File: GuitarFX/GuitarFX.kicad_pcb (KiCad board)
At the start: 4 copper layers, 149 parts, among them IC401 PCM3060PWR, J202 Screw_Terminal_01x02, J301 USB_C_Receptacle_USB2.0, J302 Conn_ARM_SWD_TagConnect_TC2030, J303 Screw_Terminal_01x06, J401 Screw_Terminal_01x04, SW301 SW_SPDT, U201 NCP718xSN500, U202 NCP1117-3.3_SOT223, U301 USBLC6-2SC6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

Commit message: Finished rough layout for MCU
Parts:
- C302: footprint Capacitor_SMD:C_0603_1608Metric -> Capacitor_SMD:C_0402_1005Metric
- moved U301 147.8 mm to (211.2, 48.5), turned to 180 degrees
- moved J301 129.8 mm to (219.2, 48.2), turned to 90 degrees
- moved C319 128.8 mm to (194.8, 53.0), turned to 135 degrees
- moved C318 123.9 mm to (200.2, 69.5), turned to -135 degrees
- moved R311 123.3 mm to (199.0, 57.2), turned to 45 degrees
- moved R310 122.2 mm to (200.2, 58.5), turned to 45 degrees
- moved R309 121.3 mm to (201.5, 59.8), turned to 45 degrees
- moved R304 120.2 mm to (212.9, 45.5), turned to 90 degrees
- moved C317 120.0 mm to (205.5, 55.2), turned to 135 degrees
- moved D302 118.0 mm to (182.4, 53.7), turned to 135 degrees
- moved R305 117.8 mm to (185.2, 50.7), turned to 135 degrees
- moved R 117.6 mm to (183.9, 52.0), turned to 135 degrees
- moved C306 116.6 mm to (202.0, 67.3), turned to -135 degrees
- moved R303 115.2 mm to (212.9, 51.5), turned to -90 degrees
- moved R307 114.6 mm to (180.7, 55.2), turned to 135 degrees
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- renumbered R306 to R

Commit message: Changed to mono input, and finished rough Analog Frontend layout
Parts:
- removed C411, C417, C425, C435: 1n, Capacitor_SMD:C_0603_1608Metric
- removed C412, C413, C426, C427: 100n, Capacitor_SMD:C_0402_1005Metric
- removed C414: 10n, Capacitor_SMD:C_0402_1005Metric
- removed C415, C434: 4.7u, Capacitor_SMD:C_0603_1608Metric
- removed C416, C418, C436: 150p, Capacitor_SMD:C_0603_1608Metric
- removed D402, D404: SMAJ15A, Diode_SMD:D_SMA
- removed R: 33R, Resistor_SMD:R_0603_1608Metric
- removed R411: 1k, Resistor_SMD:R_0402_1005Metric
- removed R412, R430: 8.2k, Resistor_SMD:R_0402_1005Metric
- removed R413, R431: 27k, Resistor_SMD:R_0402_1005Metric
- removed R414, R432: 15k, Resistor_SMD:R_0402_1005Metric
- removed R415, R433: 100R, Resistor_SMD:R_0402_1005Metric
- removed R416: 1M, Resistor_SMD:R_0402_1005Metric
- removed R434: 10k, Resistor_SMD:R_0402_1005Metric
- removed U404, U405, U408, U409: TLV9161IDBVR, TLV9161IDBVR:SOT95P280X145-5N
- added J402: Screw_Terminal_01x02, TerminalBlock_Phoenix:TerminalBlock_Phoenix_MPT-0,5-2-2.54_1x02_P2.54mm_Horizontal, F.Cu at (168.0, 105.4)
- added R306: 33R, Resistor_SMD:R_0603_1608Metric, F.Cu at (184.0, 52.0)
- C401, C419: footprint Capacitor_SMD:C_0603_1608Metric -> Capacitor_SMD:C_0402_1005Metric
- J401: value Screw_Terminal_01x04 -> Screw_Terminal_01x02; footprint TerminalBlock_Phoenix:TerminalBlock_Phoenix_MPT-0,5-4-2.54_1x04_P2.54mm_Horizontal -> TerminalBlock_Phoenix:TerminalBlock_Phoenix_MPT-0,5-2-2.54_1x02_P2.54mm_Horizontal
- R405, R406, R407, R421, R422, R423: footprint Resistor_SMD:R_0402_1005Metric -> Resistor_SMD:R_0603_1608Metric
- R410: value 1M -> 100k
- R417, R418: value 4.7k -> 10k
- moved C408 126.3 mm to (208.2, 110.9)
- moved C409 119.4 mm to (201.5, 111.7), turned to -90 degrees
- moved U402 116.9 mm to (204.8, 108.2)
- moved C401 112.2 mm to (192.2, 108.2), turned to -90 degrees
- moved C407 111.2 mm to (193.2, 105.7)
- moved C410 110.7 mm to (194.5, 107.9)
- moved R404 110.5 mm to (208.2, 108.2), turned to 180 degrees
- moved R409 109.8 mm to (208.2, 109.4), turned to 180 degrees
- moved U403 109.8 mm to (198.2, 108.2)
- moved R402 108.7 mm to (203.5, 111.0), turned to 180 degrees
- moved D401 108.6 mm to (211.8, 108.2), turned to -90 degrees
- moved J401 107.6 mm to (217.8, 108.3), turned to 90 degrees
- moved R405 103.6 mm to (201.5, 108.5), turned to -90 degrees
- moved R406 101.5 mm to (199.0, 110.9), turned to 180 degrees
- moved C430 100.8 mm to (192.7, 98.5), turned to 180 degrees
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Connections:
- net /Codec/AUDIO_VOUTL renamed /Codec/AUDIO_VOUT
- net /Codec/CODEC_VOUTL renamed /Codec/CODEC_VOUT
- net /Codec/IN_AA_BUFF_IN_L renamed /Codec/IN_AA_BUFF_IN
- net /Codec/IN_AA_BUFF_OUT_L renamed /Codec/IN_AA_BUFF_OUT
- net /Codec/IN_BUF_IN_L renamed /Codec/IN_BUF_IN
- net /Codec/IN_BUF_OUT_L renamed /Codec/IN_BUF_OUT
- net /Codec/IN_RF_L renamed /Codec/IN_RF
- net /Codec/OUT_AA_BUFF_IN_L renamed /Codec/OUT_AA_BUFF_IN
- net /Codec/OUT_AA_BUFF_OUT_L renamed /Codec/OUT_AA_BUFF_OUT
- net Net-(U406--) renamed /Codec/OUT_BUF_OUT
- C407 pad 1: /Codec/CODEC_VINL -> /Codec/CODEC_VIN
- D401 pad 1: /Codec/AUDIO_VINL -> /Codec/AUDIO_VIN
- IC401 pad 18: /Codec/CODEC_VOUTR -> Net-(IC401-VOUTR+)
- IC401 pad 25: /Codec/CODEC_VINL -> /Codec/CODEC_VIN
- IC401 pad 26: /Codec/CODEC_VINR -> /Codec/CODEC_VIN
- J401 pad 2: /Codec/AUDIO_VINR -> /Codec/AUDIO_VIN
- R404 pad 1: /Codec/AUDIO_VINL -> /Codec/AUDIO_VIN
- R410 pad 1: /Codec/IN_BUF_IN_R -> Net-(IC401-VOUTR+)
- R410 pad 2: VCOM -> GND

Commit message: Finished rough layout
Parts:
- removed D301: SMAJ15A, Diode_SMD:D_SMA
- C409: footprint Capacitor_SMD:C_0603_1608Metric -> Capacitor_SMD:C_0402_1005Metric
- R201: footprint Resistor_SMD:R_0603_1608Metric -> Resistor_SMD:R_0805_2012Metric
- moved FB302 83.4 mm to (164.2, 75.7), turned to 180 degrees
- moved C313 82.9 mm to (163.8, 69.9)
- moved C311 76.5 mm to (165.2, 77.7), turned to -90 degrees
- moved R401 76.5 mm to (152.0, 123.9), turned to 90 degrees
- moved U401 76.2 mm to (154.5, 122.8), turned to -90 degrees
- moved C312 76.1 mm to (163.2, 77.7), turned to -90 degrees
- moved R403 71.8 mm to (152.0, 121.7), turned to 90 degrees
- moved C405 69.3 mm to (154.5, 119.4)
- moved R421 68.1 mm to (136.0, 130.9), turned to -90 degrees
- moved C419 67.9 mm to (126.8, 130.7), turned to -90 degrees
- moved R422 67.6 mm to (133.5, 133.4), turned to 180 degrees
- moved C424 64.6 mm to (129.0, 130.4)
- moved C422 64.2 mm to (127.8, 128.2)
- moved R423 64.1 mm to (129.8, 132.9), turned to 90 degrees
- moved R410 62.6 mm to (140.8, 120.9), turned to 180 degrees
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
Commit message: Added mounting holes
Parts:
- added H101: MountingHole_Pad, MountingHole:MountingHole_3.2mm_M3_Pad, F.Cu at (115.0, 63.5)
- added H102: MountingHole_Pad, MountingHole:MountingHole_3.2mm_M3_Pad, F.Cu at (175.0, 63.5)
- added H103: MountingHole_Pad, MountingHole:MountingHole_3.2mm_M3_Pad, F.Cu at (175.0, 138.5)
- added H104: MountingHole_Pad, MountingHole:MountingHole_3.2mm_M3_Pad, F.Cu at (115.0, 138.5)
- moved C311 1.39 mm to (165.2, 79.0)
- moved C312 1.39 mm to (163.2, 79.0)
- moved C313 1.39 mm to (163.8, 71.3)
- moved FB302 1.39 mm to (164.2, 77.0)
- moved FL301 1.39 mm to (159.9, 73.9)
- moved J301 1.39 mm to (173.0, 73.5)
- moved R303 1.39 mm to (166.7, 76.8)
- moved R304 1.39 mm to (166.7, 70.8)
- moved U301 1.39 mm to (164.9, 73.8)
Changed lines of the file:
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@@
     )
   )
+  (footprint "MountingHole:MountingHole_3.2mm_M3_Pad" (layer "F.Cu")
+    (at 175 63.5)
+    (descr "Mounting Hole 3.2mm, M3")
+    (tags "mounting hole 3.2mm m3")
+    (property "Sheetfile" "GuitarFX.kicad_sch")
+    (property "Sheetname" "")
+    (property "ki_description" "Mounting Hole with connection")
+    (property "ki_keywords" "mounting hole")
+    (attr exclude_from_pos_files)
+    (fp_text reference "H102" (at 0 -4.2) (layer "F.SilkS") hide
+        (effects (font (size 1 1) (thickness 0.15)))
+    )
+    (fp_text value "MountingHole_Pad" (at 0 4.2) (layer "F.Fab")
+        (effects (font (size 1 1) (thickness 0.15)))
+    )
+    (fp_text user "${REFERENCE}" (at 0 0) (layer "F.Fab")
+        (effects (font (size 1 1) (thickness 0.15)))
+    )
+    (fp_circle (center 0 0) (end 3.2 0)
+      (stroke (width 0.15) (type solid)) (fill none) (layer "Cmts.User"))
+    (fp_circle (center 0 0) (end 3.45 0)
+      (stroke (width 0.05) (type solid)) (fill none) (layer "F.CrtYd"))
+    (pad "1" thru_hole circle (at 0 0) (size 6.4 6.4) (drill 3.2) (layers "*.Cu" "*.Mask")
+      (net 2 "GND") (pinfunction "1") (pintype "input"))
+  )
   (footprint "Resistor_SMD:R_0402_1005Metric" (layer "F.Cu")
     (at 164.04 131.365 180)
@@
     )
   )
+  (footprint "MountingHole:MountingHole_3.2mm_M3_Pad" (layer "F.Cu")
+    (at 175 138.5)
+    (descr "Mounting Hole 3.2mm, M3")
+    (tags "mounting hole 3.2mm m3")
+    (property "Sheetfile" "GuitarFX.kicad_sch")
+    (property "Sheetname" "")
+    (property "ki_description" "Mounting Hole with connection")
+    (property "ki_keywords" "mounting hole")
+    (attr exclude_from_pos_files)
+    (fp_text reference "H103" (at 0 -4.2) (layer "F.SilkS") hide
+        (effects (font (size 1 1) (thickness 0.15)))
+    )
+    (fp_text value "MountingHole_Pad" (at 0 4.2) (layer "F.Fab")
+        (effects (font (size 1 1) (thickness 0.15)))
+    )
+    (fp_text user "${REFERENCE}" (at 0 0) (layer "F.Fab")
+        (effects (font (size 1 1) (thickness 0.15)))
+    )
+    (fp_circle (center 0 0) (end 3.2 0)
+      (stroke (width 0.15) (type solid)) (fill none) (layer "Cmts.User"))
+    (fp_circle (center 0 0) (end 3.45 0)
+      (stroke (width 0.05) (type solid)) (fill none) (layer "F.CrtYd"))
+    (pad "1" thru_hole circle (at 0 0) (size 6.4 6.4) (drill 3.2) (layers "*.Cu" "*.Mask")
+      (net 2 "GND") (pinfunction "1") (pintype "input"))
+  )
   (footprint "Diode_SMD:D_SOD-123" (layer "F.Cu")
     (at 162.75 107.41 90)
@@
   )
   (footprint "Resistor_SMD:R_0402_1005Metric" (layer "F.Cu")
-    (at 166.69 75.4 -90)
+    (at 166.69 76.79 -90)
     (descr "Resistor SMD 0402 (1005 Metric), square (rectangular) end terminal, IPC_7351 nominal, (Body size source: IPC-SM-782 page 72, https://www.pcb-3d.com/wordpress/wp-content/uploads/ipc-sm-782a_amendment_1_and_2.pdf), generated with kicad-footprint-generator")
     (tags "resistor")
@@
   )
   (footprint "Inductor_SMD:L_0603_1608Metric" (layer "F.Cu")
-    (at 164.25 75.66 180)
+    (at 164.25 77.05 180)
     (descr "Inductor SMD 0603 (1608 Metric), square (rectangular) end terminal, IPC_7351 nominal, (Body size source: http://www.tortai-tech.com/upload/download/2011102023233369053.pdf), generated with kicad-footprint-generator")
     (tags "inductor")
@@
   )
   (footprint "ACM2012-900-2P-TL002:ACM20129002PTL002" (layer "F.Cu")
-    (at 159.865 72.51 180)
+    (at 159.865 73.9 180)
     (descr "ACM2012-900-2P-TL002-2")
     (tags "Filter")
@@
     )
   )
+  (footprint "MountingHole:MountingHole_3.2mm_M3_Pad" (layer "F.Cu")
+    (at 115 138.5)
+    (descr "Mounting Hole 3.2mm, M3")
+    (tags "mounting hole 3.2mm m3")
+    (property "Sheetfile" "GuitarFX.kicad_sch")
+    (property "Sheetname" "")
+    (property "ki_description" "Mounting Hole with connection")
+    (property "ki_keywords" "mounting hole")
+    (attr exclude_from_pos_files)
+    (fp_text reference "H104" (at 0 -4.2) (layer "F.SilkS") hide
+        (effects (font (size 1 1) (thickness 0.15)))
+    )
+    (fp_text value "MountingHole_Pad" (at 0 4.2) (layer "F.Fab")
+        (effects (font (size 1 1) (thickness 0.15)))
+    )
+    (fp_text user "${REFERENCE}" (at 0 0) (layer "F.Fab")
+        (effects (font (size 1 1) (thickness 0.15)))
+    )
+    (fp_circle (center 0 0) (end 3.2 0)
+      (stroke (width 0.15) (type solid)) (fill none) (layer "Cmts.User"))
+    (fp_circle (center 0 0) (end 3.45 0)
+      (stroke (width 0.05) (type solid)) (fill none) (layer "F.CrtYd"))
+    (pad "1" thru_hole circle (at 0 0) (size 6.4 6.4) (drill 3.2) (layers "*.Cu" "*.Mask")
+      (net 2 "GND") (pinfunction "1") (pintype "input"))
+  )
   (footprint "Capacitor_SMD:C_0603_1608Metric" (layer "F.Cu")
     (at 150.29 129.84)
@@
   )
   (footprint "Capacitor_SMD:C_0402_1005Metric" (layer "F.Cu")
-    (at 163.25 77.66 -90)
+    (at 163.25 79.05 -90)
     (descr "Capacitor SMD 0402 (1005 Metric), square (rectangular) end terminal, IPC_7351 nominal, (Body size source: IPC-SM-782 page 76, https://www.pcb-3d.com/wordpress/wp-content/uploads/ipc-sm-782a_amendment_1_and_2.pdf), generated with kicad-footprint-generator")
     (tags "capacitor")
@@
   )
   (footprint "Capacitor_SMD:C_0402_1005Metric" (layer "F.Cu")
-    (at 163.77 69.91)
+    (at 163.77 71.3)
     (descr "Capacitor SMD 0402 (1005 Metric), square (rectangular) end terminal, IPC_7351 nominal, (Body size source: IPC-SM-782 page 76, https://www.pcb-3d.com/wordpress/wp-content/uploads/ipc-sm-782a_amendment_1_and_2.pdf), generated with kicad-footprint-generator")
     (tags "capacitor")
@@
   )
   (footprint "Capacitor_SMD:C_0402_1005Metric" (layer "F.Cu")
-    (at 165.25 77.66 -90)
+    (at 165.25 79.05 -90)
     (descr "Capacitor SMD 0402 (1005 Metric), square (rectangular) end terminal, IPC_7351 nominal, (Body size source: IPC-SM-782 page 76, https://www.pcb-3d.com/wordpress/wp-content/uploads/ipc-sm-782a_amendment_1_and_2.pdf), generated with kicad-footprint-generator")
     (tags "capacitor")
@@
     )
   )
+  (footprint "MountingHole:MountingHole_3.2mm_M3_Pad" (layer "F.Cu")
+    (at 115 63.5)
+    (descr "Mounting Hole 3.2mm, M3")
+    (tags "mounting hole 3.2mm m3")
+    (property "Sheetfile" "GuitarFX.kicad_sch")
+    (property "Sheetname" "")
+    (property "ki_description" "Mounting Hole with connection")
+    (property "ki_keywords" "mounting hole")
+    (attr exclude_from_pos_files)
+    (fp_text reference "H101" (at 0 -4.2) (layer "F.SilkS") hide
+        (effects (font (size 1 1) (thickness 0.15)))
+    )
+    (fp_text value "MountingHole_Pad" (at 0 4.2) (layer "F.Fab")
+        (effects (font (size 1 1) (thickness 0.15)))
+    )
+    (fp_text user "${REFERENCE}" (at 0 0) (layer "F.Fab")
+        (effects (font (size 1 1) (thickness 0.15)))
+    )
+    (fp_circle (center 0 0) (end 3.2 0)
+      (stroke (width 0.15) (type solid)) (fill none) (layer "Cmts.User"))
+    (fp_circle (center 0 0) (end 3.45 0)
+      (stroke (width 0.05) (type solid)) (fill none) (layer "F.CrtYd"))
+    (pad "1" thru_hole circle (at 0 0) (size 6.4 6.4) (drill 3.2) (layers "*.Cu" "*.Mask")
+      (net 2 "GND") (pinfunction "1") (pintype "input"))
+  )
   (footprint "Capacitor_SMD:C_0603_1608Metric" (layer "F.Cu")
     (at 148.5 76.91 135)
@@
   )
   (footprint "Resistor_SMD:R_0402_1005Metric" (layer "F.Cu")
-    (at 166.69 69.41 90)
+    (at 166.69 70.8 90)
     (descr "Resistor SMD 0402 (1005 Metric), square (rectangular) end terminal, IPC_7351 nominal, (Body size source: IPC-SM-782 page 72, https://www.pcb-3d.com/wordpress/wp-content/uploads/ipc-sm-782a_amendment_1_and_2.pdf), generated with kicad-footprint-generator")
     (tags "resistor")
@@
   )
   (footprint "Package_TO_SOT_SMD:SOT-23-6" (layer "F.Cu")
-    (at 164.94 72.41 180)
+    (at 164.94 73.8 180)
     (descr "SOT, 6 Pin (https://www.jedec.org/sites/default/files/docs/Mo-178c.PDF variant AB), generated with kicad-footprint-generator ipc_gullwing_generator.py")
     (tags "SOT TO_SOT_SMD")
@@
   )
   (footprint "Connector_USB:USB_C_Receptacle_HRO_TYPE-C-31-M-12" (layer "F.Cu")
-    (at 173 72.16 90)
+    (at 173 73.55 90)
     (descr "USB Type-C receptacle for USB 2.0 and PD, http://www.krhro.com/uploads/soft/180320/1-1P320120243.pdf")
     (tags "usb usb-c 2.0 pd")

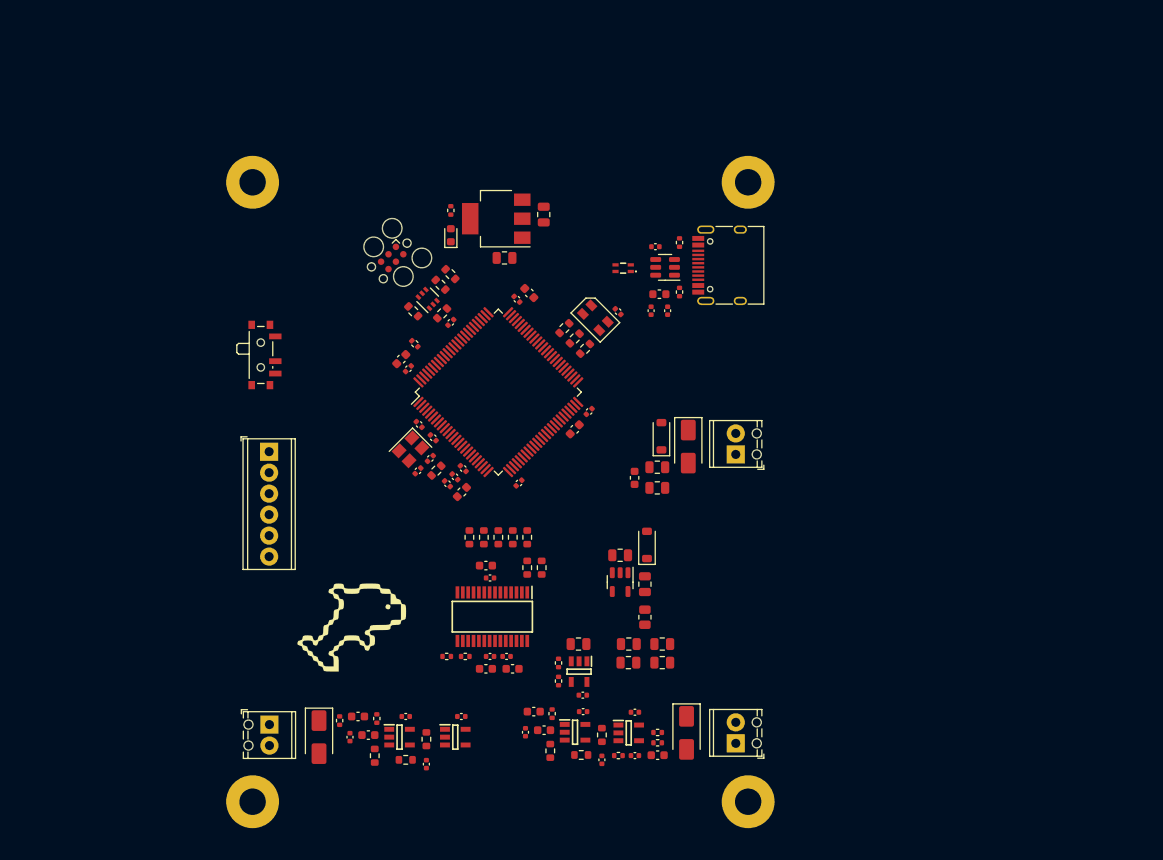
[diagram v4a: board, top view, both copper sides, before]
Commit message: Made position changes to nicer coordinates, and added edge cuts
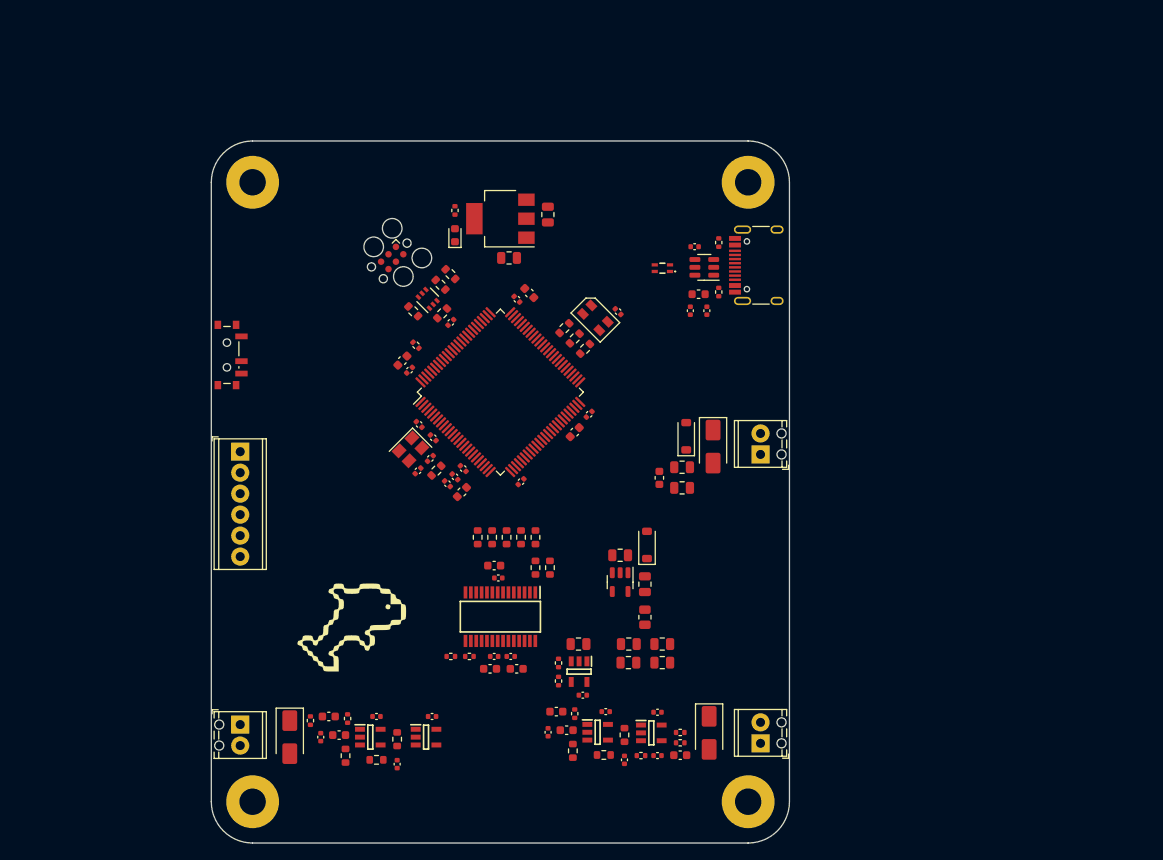
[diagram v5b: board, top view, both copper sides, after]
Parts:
- moved C311 4.75 mm to (170.0, 79.0)
- moved C312 4.75 mm to (168.0, 79.0)
- moved C313 4.75 mm to (168.5, 71.3)
- moved FB302 4.75 mm to (169.0, 77.0)
- moved FL301 4.75 mm to (164.6, 73.9)
- moved R303 4.75 mm to (171.4, 76.8)
- moved R304 4.75 mm to (171.4, 70.8)
- moved U301 4.75 mm to (169.7, 73.8)
- moved J301 4.45 mm to (177.4, 73.5)
- moved SW301 4.10 mm to (112.2, 84.4)
- moved C420 3.54 mm to (136.7, 128.2)
- moved C419 3.54 mm to (123.2, 130.7)
- moved C422 3.54 mm to (124.2, 128.2)
- moved D403 3.54 mm to (119.5, 130.7)
- moved J402 3.54 mm to (113.5, 129.2)
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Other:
- board outline added: 70 x 85 mm

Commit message: Pre routing commit
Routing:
- added copper zone on In1.Cu, net GND
- added copper zone on In2.Cu, net GND
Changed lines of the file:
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@@
       (layer "B.Paste" (type "Bottom Solder Paste"))
       (layer "B.SilkS" (type "Bottom Silk Screen"))
-      (copper_finish "ENIG")
+      (copper_finish "None")
       (dielectric_constraints no)
     )
@@
   (gr_line (start 115 58.5) (end 175 58.5)
     (stroke (width 0.1) (type default)) (layer "Edge.Cuts"))
+  (zone (net 2) (net_name "GND") (layers "In1.Cu" "In2.Cu") (hatch edge 0.5)
+    (connect_pads (clearance 0.4))
+    (min_thickness 0.3) (filled_areas_thickness no)
+    (fill yes (thermal_gap 0.5) (thermal_bridge_width 0.5))
+    (polygon
+      (pts
+        (xy 108.5 56.5)
+        (xy 181 56.5)
+        (xy 181 144.5)
+        (xy 108.5 144.5)
+      )
+    )
+  )
 )
